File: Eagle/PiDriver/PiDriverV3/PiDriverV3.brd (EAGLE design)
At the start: 78.4 x 92.7 mm, 47 parts, among them IC1 L293E, IC2 L293E

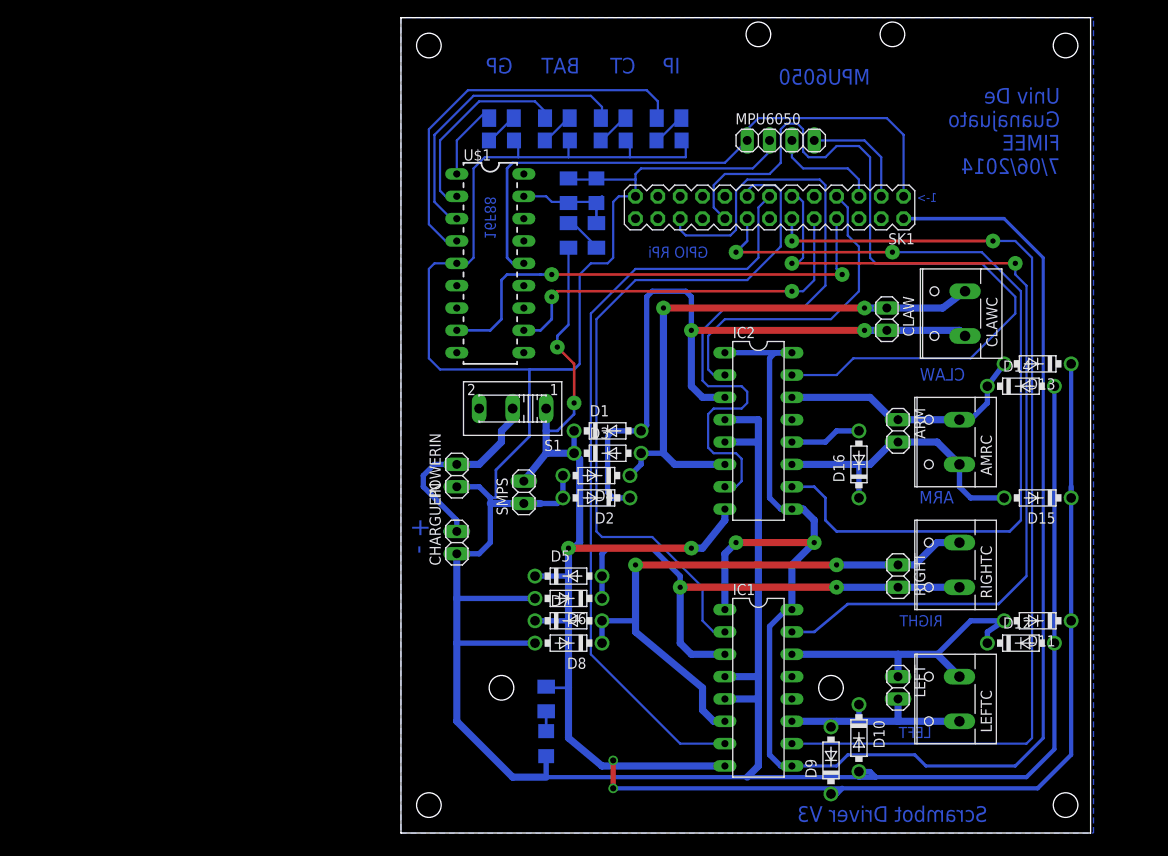
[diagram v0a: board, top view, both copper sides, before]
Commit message: A second quote of smps for PiDrive was added
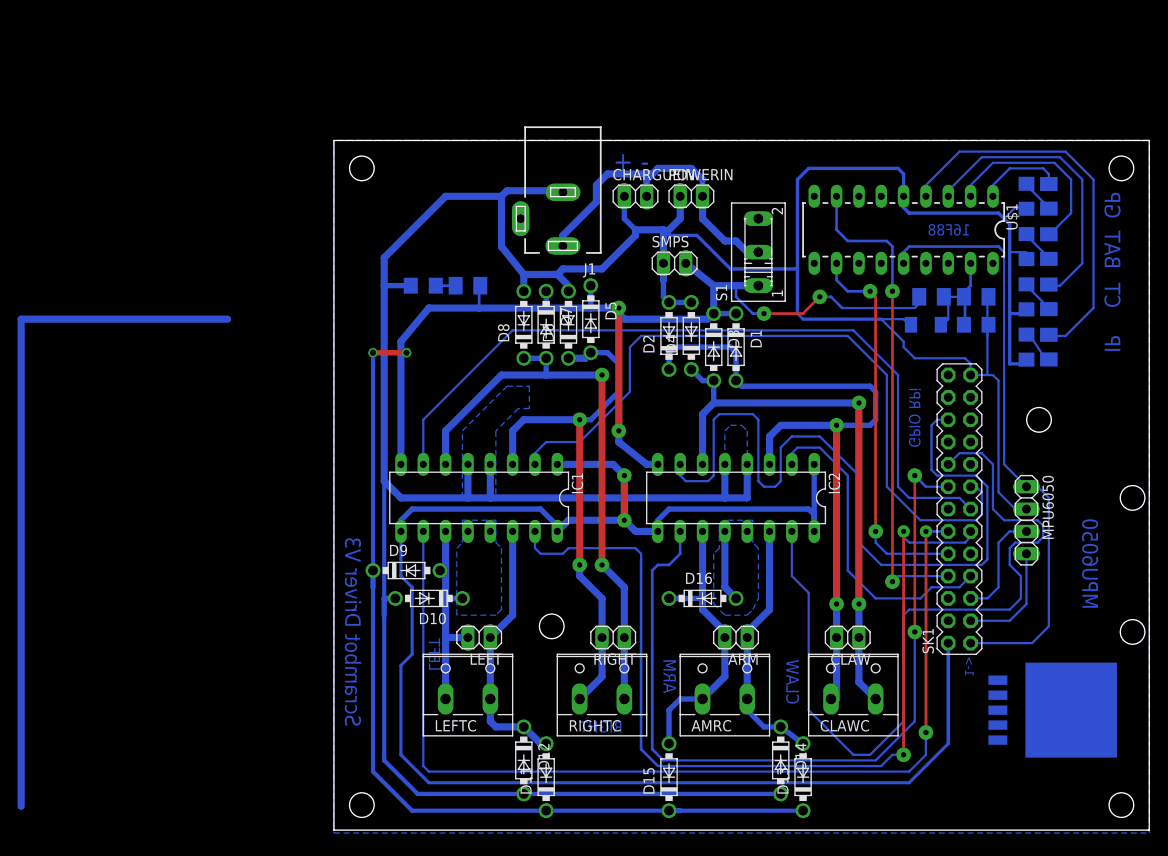
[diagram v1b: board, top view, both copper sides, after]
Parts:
- removed LED1: (no value), led:1206
- removed R4: 1k, rcl:M1206
- added D17: BZV55-C3V3, diode:SOD80C
- added IC3: (no value), linear:TO263-5
- added J1: DCJ0202, con-jack:DCJ0202
- added POWER: (no value), led:1206
- R1: value (none) -> 1.5k
- R3: value 1k -> 2k
- R5, R6, R7, R8: value (none) -> 220
- moved R5 62.9 mm to (81.3, 72.4), turned to 90 degrees
- moved LED2 60.0 mm to (78.7, 72.4), turned to 270 degrees
- moved D11 58.6 mm to (24.1, 6.35), turned to 90 degrees
- moved D12 58.1 mm to (21.6, 8.26), turned to 270 degrees
- moved R6 57.8 mm to (81.3, 66.7), turned to 90 degrees
- moved LEFTC 55.2 mm to (15.2, 15.9), turned to 0 degrees
- moved LED3 54.7 mm to (78.7, 66.7), turned to 270 degrees
- moved D13 54.0 mm to (53.3, 6.35), turned to 90 degrees
- moved R7 53.5 mm to (81.3, 61.0), turned to 90 degrees
- moved D9 52.9 mm to (8.26, 29.8), turned to 0 degrees
- moved D15 52.6 mm to (38.1, 6.35), turned to 90 degrees
- moved MPU6050 51.4 mm to (78.7, 35.6), turned to 270 degrees
- moved D10 51.4 mm to (10.8, 26.7), turned to 180 degrees
- moved D14 50.6 mm to (50.8, 8.26), turned to 270 degrees
- moved R8 50.4 mm to (81.3, 55.2), turned to 90 degrees
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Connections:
- removed net N$25: C1.1, R2.2, R4.2, U$1.17
- net GND: now also D17.A, IC3.3, IC3.6, J1.3, POWER.C; no longer LED1.C
- net N$1: now also POWER.A; no longer LED1.A
- net N$28: now also C1.1, D17.C, R2.2, U$1.17; no longer R4.1
- net N$3: now also J1.1
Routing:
- net N$22: track 0.00 -> 78.9 mm
- net N$3: track 24.0 -> 37.1 mm
- net N$25: track 12.0 -> 0.00 mm
- net N$28: track 0.00 -> 8.78 mm
- net N$20: track 81.5 -> 88.9 mm
- net VCC: track 184.9 -> 179.3 mm
- net N$14: track 35.4 -> 30.0 mm
- net N$27: track 5.13 -> 0.00 mm
- net N$16: track 0.00 -> 4.71 mm
- net N$26: track 100.0 -> 104.2 mm
- net N$6: track 94.8 -> 91.3 mm
- net GND: track 389.9 -> 393.0 mm
- net N$10: track 225.2 -> 222.9 mm
- net RA2: track 8.30 -> 9.94 mm
- net RA5: track 45.7 -> 44.2 mm
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- added copper zone on layer 16, net GND
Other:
- board size 78.4 x 92.7 mm -> 92.7 x 78.4 mm
- board text removed: "Univ De Guanajuato FIMEE 7/06/2014"

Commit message: An SMPS and Ref Voltage was added to PiDrive
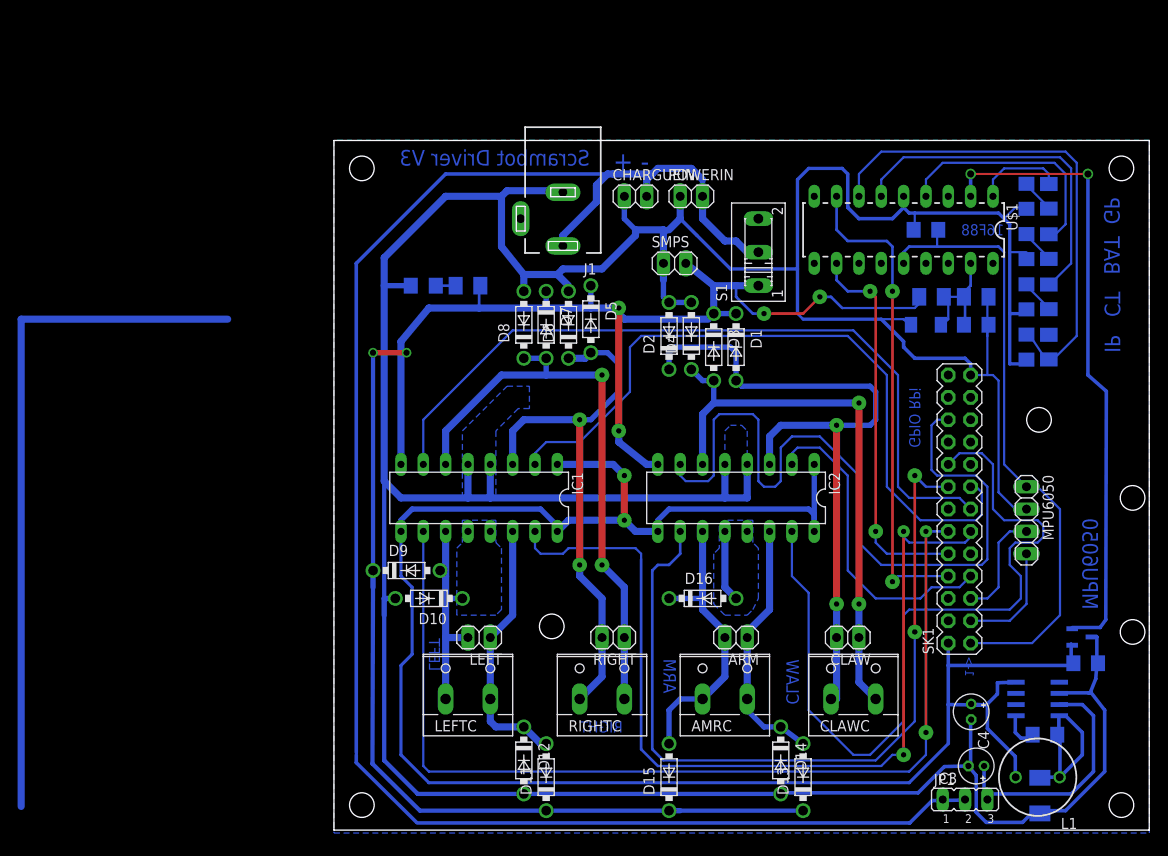
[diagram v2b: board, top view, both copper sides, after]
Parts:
- removed IC3: (no value), linear:TO263-5
- added C2: (no value), rcl:C1206
- added C3: 100 uF MCGPR25V107M6.3X11, rcl:E1,8-4
- added C4: 68 uF 10MS568MEFC6.3X5, rcl:E1,8-4
- added C5: 10 nF CC1206KRX7R9BB103, rcl:C1206
- added C6: 0.47 uF C1206C474K5RACTU, rcl:C1206
- added D18: (no value), diode:DO-214AC
- added JP1: (no value), jumper:JP2
- added L1: 47 uH 13R473C, rcl:6000-XXXX-RC
- added U1: LM2675M-5.0, LM2675M-5.0:SOIC127P620X175-8N
- added U2: REF3033AIDBZT, TI-REF3033AIDBZT:SOT95P237X112-3N
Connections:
- net RA2 renamed N$15
- removed net N$15 (its old number): R6.2, U$1.2
- removed net RA4: R7.2, U$1.3
- removed net RA5: R8.2, U$1.4
- new net N$25: C5.2, D18.C, L1.1, U1.8
- new net N$27: C3.+, JP1.3, U1.7
- new net N$31: R6.2, U$1.4
- new net N$40: C5.1, U1.1
- new net N$42: R7.2, U$1.6
- new net N$45: C1.2, C2.2, C3.-, C4.-, CHARGUEIN.1, D10.A, D12.A, D14.A, D16.A, D17.A, D18.A, D2.A, D4.A, D6.A, D8.A, IC1.12, IC1.13, IC1.4, IC1.5, IC2.12, IC2.13, IC2.4, IC2.5, J1.3, LED2.C, LED3.C, LED4.C, LED5.C, MPU6050.2, POWER.C, POWERIN.1, R2.1, SK1.14, SK1.20, SK1.25, SK1.6, SK1.9, SMPS.1, U$1.5, U1.6
- new net N$48: R8.2, U$1.7
- new net N$49: U$1.2, U2.2
- net GND: now also C6.1, U2.3; no longer C1.2, CHARGUEIN.1, D10.A, D12.A, D14.A, D16.A, D17.A, D2.A, D4.A, D6.A, D8.A, IC1.12, IC1.13, IC1.4, IC1.5, IC2.12, IC2.13, IC2.4, IC2.5, IC3.3, IC3.6, J1.3, LED2.C, LED3.C, LED4.C, LED5.C, MPU6050.2, POWER.C, POWERIN.1, R2.1, SK1.14, SK1.20, SK1.25, SK1.6, SK1.9, SMPS.1, U$1.5
- net N$17: now also C2.1
- net N$3: now also JP1.1, JP1.2
- net VCC: now also C4.+, C6.2, L1.2, U1.4, U2.1
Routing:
- net N$45: track 0.00 -> 417.0 mm
- net GND: track 393.0 -> 51.1 mm
- net N$3: track 37.1 -> 126.2 mm
- net N$49: track 0.00 -> 71.8 mm, vias 0 -> 2
- net N$47: track 0.00 -> 63.5 mm
- net N$48: track 0.00 -> 52.8 mm
- net RA5: track 44.2 -> 0.00 mm
- net N$42: track 0.00 -> 39.5 mm
- net VCC: track 179.3 -> 216.6 mm
- net RA4: track 32.9 -> 0.00 mm
- net N$27: track 0.00 -> 29.6 mm
- net N$31: track 0.00 -> 27.2 mm
- net N$15 (its old number): track 21.7 -> 0.00 mm
- net N$43: track 0.00 -> 16.8 mm
- net N$46: track 0.00 -> 10.5 mm
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- added copper zone on layer 16, net N$45
- removed copper zone on layer 16, net GND

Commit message: some traces were fixed, the newark bom was added
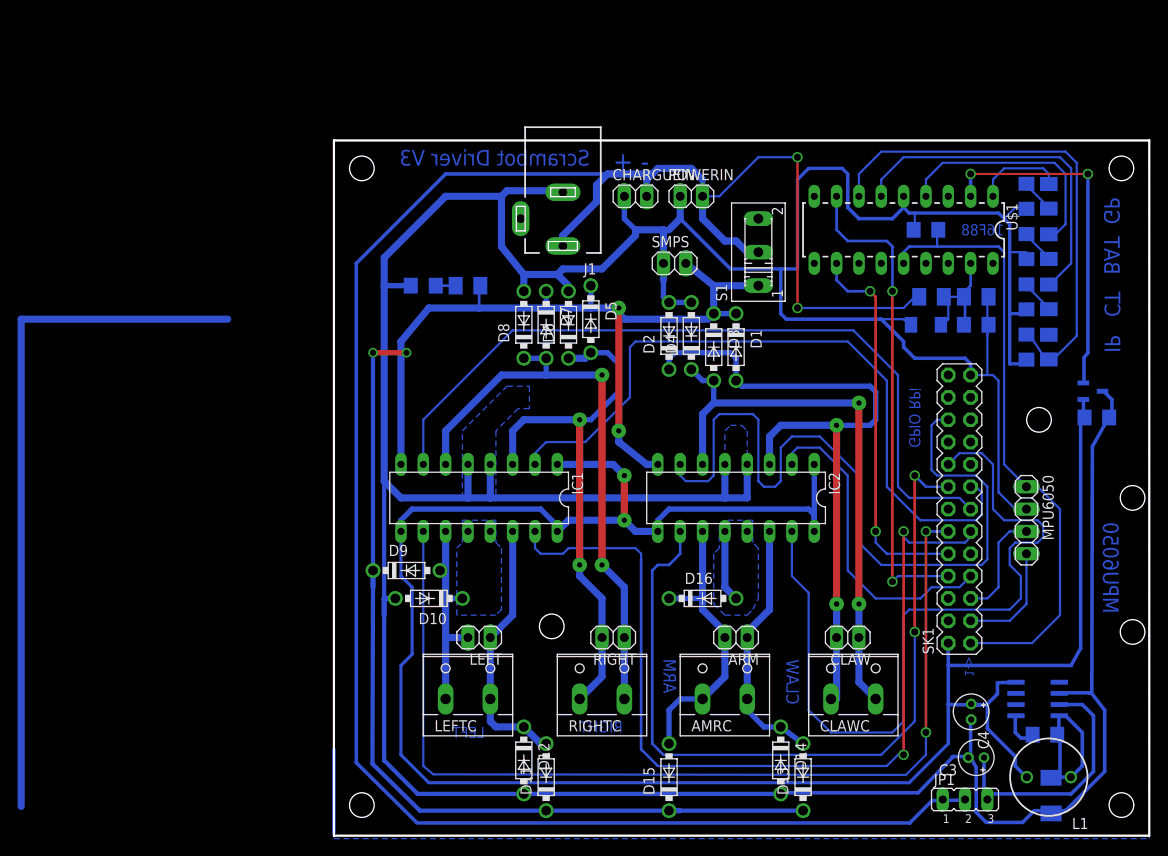
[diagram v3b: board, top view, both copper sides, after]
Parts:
- C1: value 10uF -> 10uF C1206C106K4RACTU
- C2: value (none) -> 10 nF
- C4: value 68 uF 10MS568MEFC6.3X5 -> 68 uF EKZE160ELL680MF07D
- D18: value (none) -> SSA23L-E3/61T
- R1: value 1.5k -> 4k
- R2: value 3.01k -> 422
- R3: value 2k -> 2.61k
- moved C6 28.0 mm to (86.7, 47.2)
- moved U2 28.0 mm to (86.3, 50.2)
- moved D18 1.27 mm to (81.5, 4.25)
- moved L1 1.27 mm to (81.3, 6.35)
- moved C3 0.95 mm to (73.0, 8.57)
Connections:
- removed net N$3: CHARGUEIN.2, J1.1, JP1.1, JP1.2, POWERIN.2, S1.2
- new net N$53: CHARGUEIN.2, J1.1, JP1.1, JP1.2, POWERIN.2, R3.1, S1.2
- net N$10: no longer R3.1
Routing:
- net N$53: track 0.00 -> 170.4 mm, vias 0 -> 2
- net N$3: track 126.2 -> 0.00 mm
- net N$49: track 71.8 -> 39.8 mm
- net GND: track 51.1 -> 77.3 mm
- net VCC: track 216.6 -> 242.7 mm
- net N$10: track 222.5 -> 197.2 mm, vias 6 -> 4
- net N$39: track 0.00 -> 9.50 mm
- net N$45: track 417.0 -> 420.5 mm
- net N$52: track 0.00 -> 2.15 mm
- net N$18: track 91.3 -> 89.2 mm
- net N$23: track 80.6 -> 79.3 mm
- net N$27: track 29.6 -> 30.6 mm
- net N$6: track 91.3 -> 90.4 mm
- net N$43: track 16.8 -> 15.9 mm
- net N$7: track 81.0 -> 80.5 mm
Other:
- board size 92.7 x 78.4 mm -> 92.7 x 79 mm
